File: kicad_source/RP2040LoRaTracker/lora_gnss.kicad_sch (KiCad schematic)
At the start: 32 parts, among them Q1 NTR4171P, SW3 SW_SPDT, U2 Ai-Thinker-Ra-01, U3 NEO-M8N, U5 24LC32, U6 BME280, U7 TPS3839DBZ, U8 TPS73630DBV, U9 MCP73832-2-OT

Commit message: added battery voltage measurement, R17 and R18
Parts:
- added C24: 100 nF, Capacitor_SMD:C_0603_1608Metric, symbol Device:C_Small
- added R19: 0R, Resistor_SMD:R_0603_1608Metric, symbol Device:R_Small
- D2: value LED_Small -> LED_Small blue
- D3: value LED_Small -> LED_Small red
- L1: value L -> 27 nH
- R9: value 1k -> 10R
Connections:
- net GND: now also C24.2, R19.2
- net VCC_RF_R: now reaches L1.1, R9.2
- net VCC_RF_R: now also C24.1
- net VDD_USB: now reaches U3.7 (VDD_USB)
- net VDD_USB: now also R19.1
- no-connect marks 14 -> 13
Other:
- note added: "connect VDD_USB to GND if no USB is used"
- note added: "u-Blox NEO-6M or NEO-M8N or NEO-M9N GNSS receiver"
- note removed: "u-Blox NEO-6M or NEO-M8N GNSS receiver"

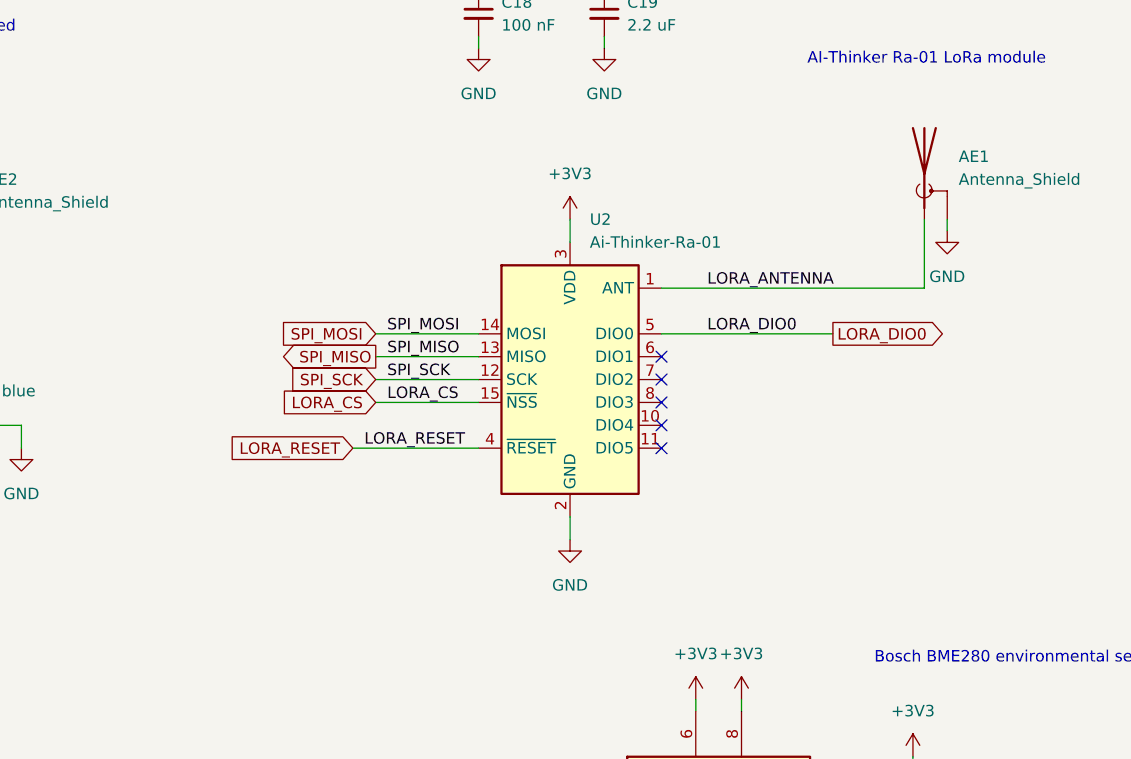
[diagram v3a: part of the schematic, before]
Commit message: added compatibility for LoRa module Ra-01S, added R20 and R21
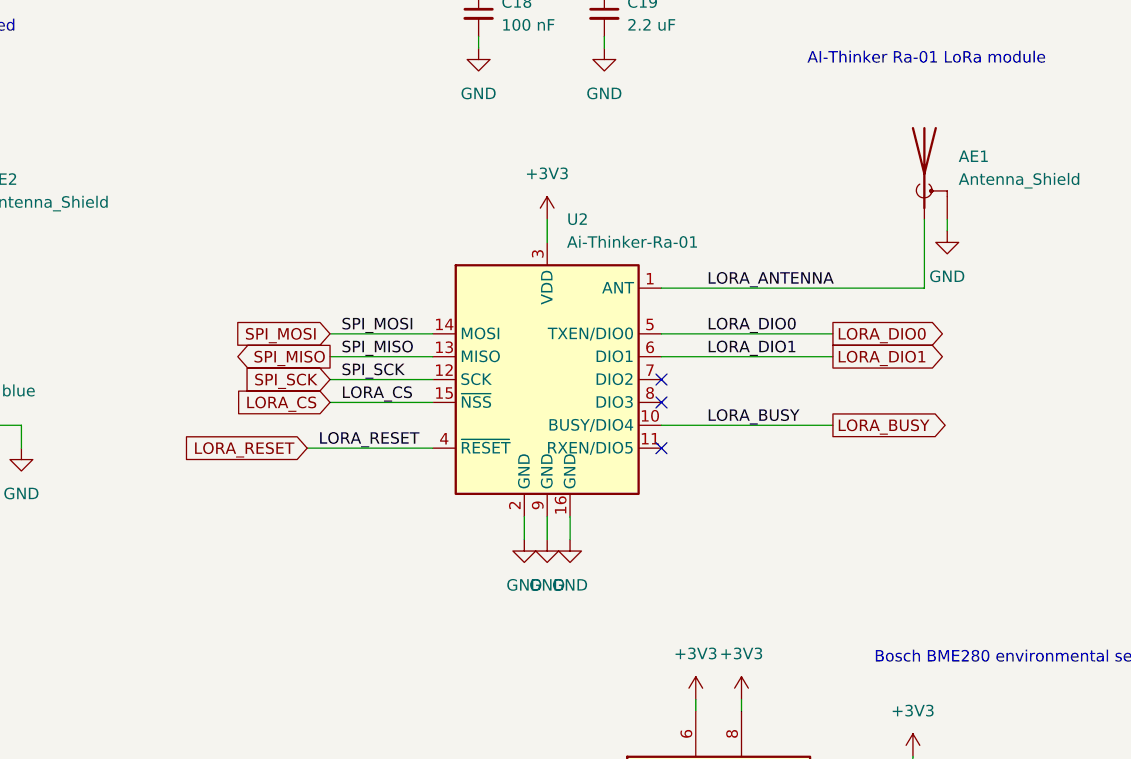
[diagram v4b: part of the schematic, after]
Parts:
- U2: symbol RF_Module:Ai-Thinker-Ra-01 -> RF_Module2:Ai-Thinker-Ra-01S
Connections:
- net LORA_BUSY: now reaches U2.10 (BUSY/DIO4)
- net LORA_DIO1: now reaches U2.6 (DIO1)
- no-connect marks 13 -> 11
